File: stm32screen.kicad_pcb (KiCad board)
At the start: 4 copper layers, 46 x 46 mm, 40 parts, among them J1 SWD, J2 GC9A01, J3 OIL, J4 PRESS, J5 POWER IN, J6 EGT, SW1 NRST, SW2 USER, U1 TS1117BCW-3.3, U2 STM32F407VETx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

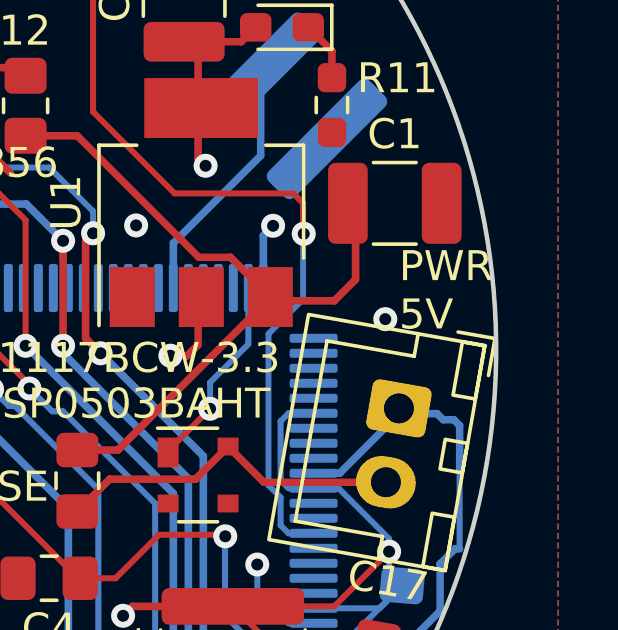
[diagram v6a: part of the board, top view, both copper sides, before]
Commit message: Changed display conn symbol, added NC flags. Corrected silkscreen labels
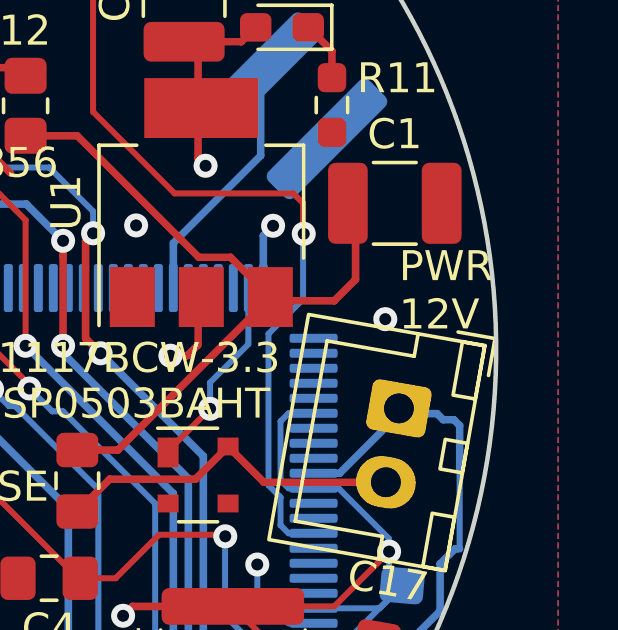
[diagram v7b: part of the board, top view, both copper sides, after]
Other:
- board text added: "PWR 12V"
- board text removed: "PWR 5V"
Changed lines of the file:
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@@
 			(net 12 "unconnected-(D1-K-Pad2)")
 			(pinfunction "K")
-			(pintype "passive")
+			(pintype "passive+no_connect")
 		)
 		(pad "3" smd rect
@@
 			(net 13 "unconnected-(D1-K-Pad3)")
 			(pinfunction "K")
-			(pintype "passive")
+			(pintype "passive+no_connect")
 		)
 		(pad "4" smd rect
@@
 			)
 		)
-		(property "Description" ""
+		(property "Description" "Generic connector, single row, 01x07, script generated (kicad-library-utils/schlib/autogen/connector/)"
 			(at 0 0 0)
 			(layer "B.Fab")
@@
 		)
 	)
-	(gr_text "PWR\n5V"
+	(gr_text "PWR\n12V"
 		(at 142.6972 71.0438 0)
 		(layer "F.SilkS")

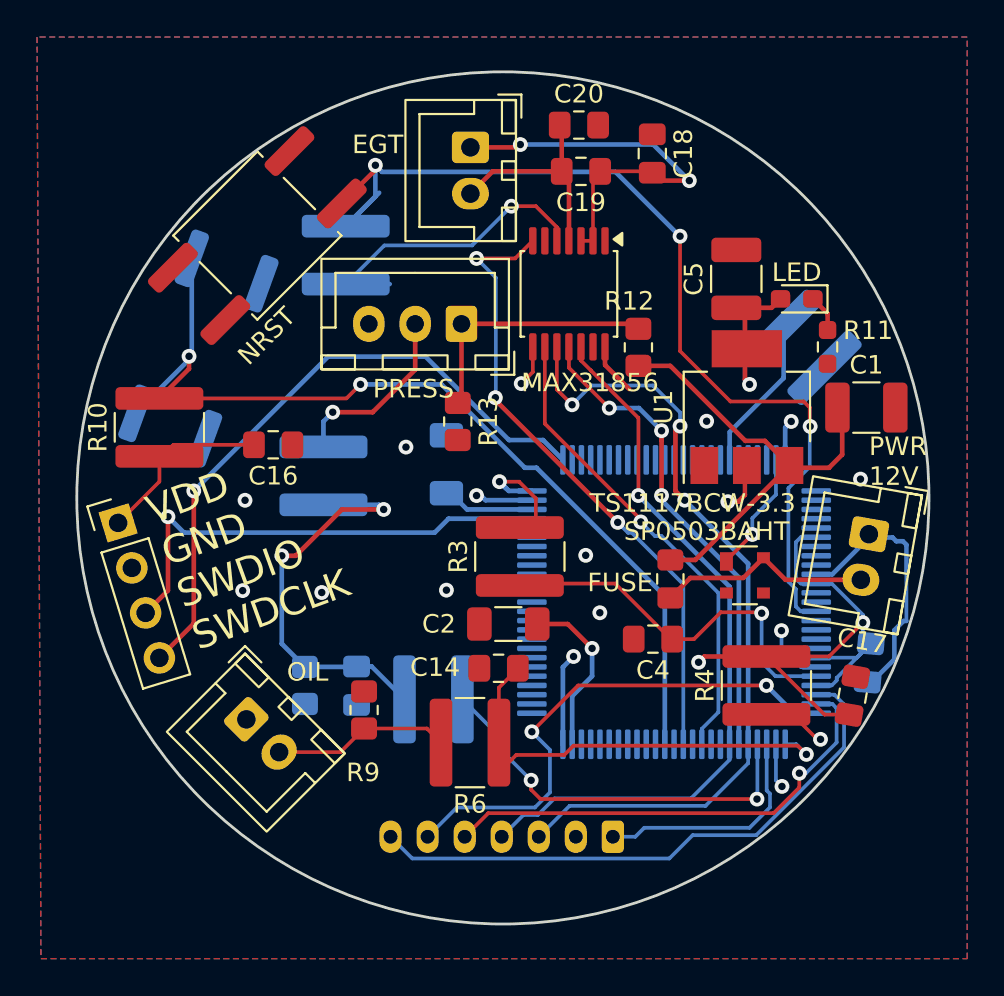
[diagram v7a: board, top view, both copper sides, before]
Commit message: Switched from SP0503BAHT to SMBJ24A for a TVS Diode, since we're using 12v supply now instead of 5v
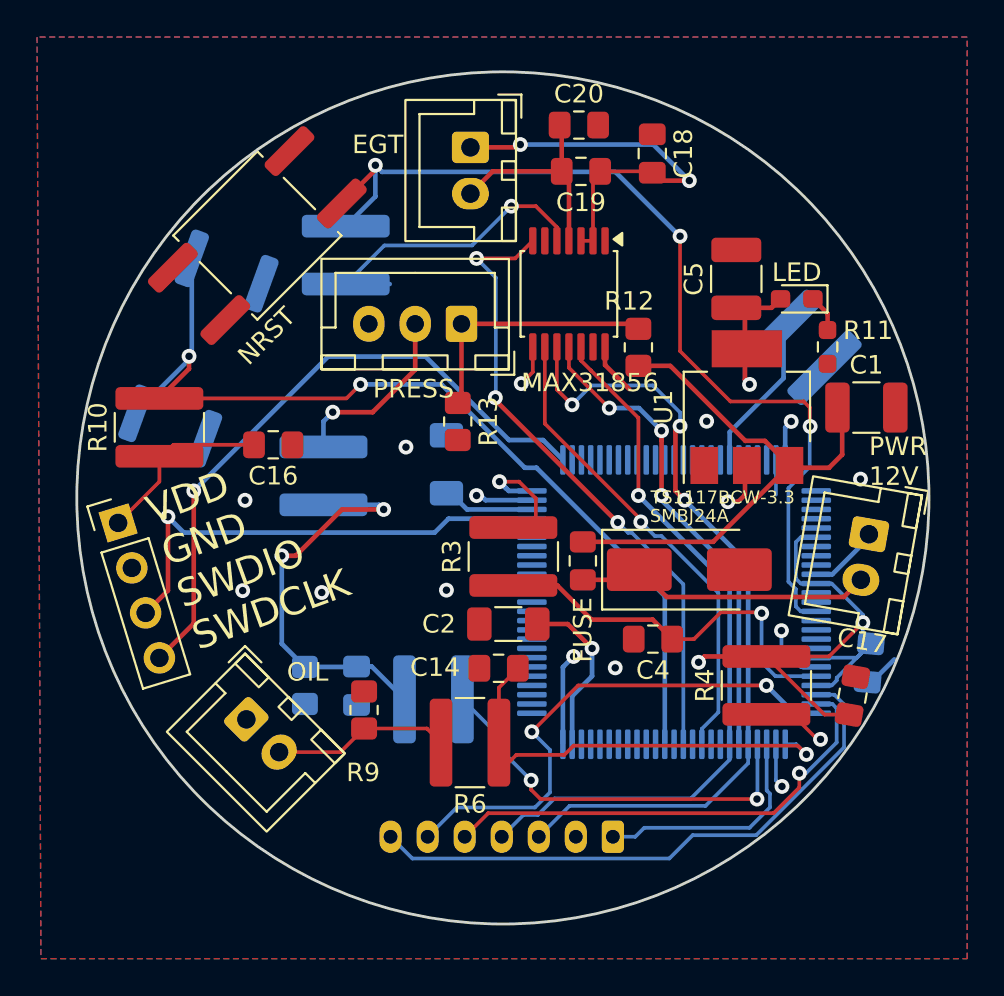
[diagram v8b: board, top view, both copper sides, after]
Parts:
- removed D1: SP0503BAHT, Package_TO_SOT_SMD:SOT-143
- added D3: SMBJ24A, Diode_SMD:D_SMB_Handsoldering, F.Cu at (133.0, 75.5)
- moved F1 4.82 mm to (127.2, 75.0)
- moved R3 0.35 mm to (123.5, 74.8)
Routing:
- net GND: track 32.8 -> 19.5 mm, vias 13 -> 11
- net Net-(D3-K): track 11.7 -> 16.2 mm
- net Vin: track 23.8 -> 28.3 mm
- net NRST: track 54.3 -> 51.8 mm
- net Net-(U2-VREF+): track 20.4 -> 21.7 mm
